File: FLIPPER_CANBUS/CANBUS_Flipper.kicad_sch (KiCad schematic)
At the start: 15 parts, among them J1 Conn_01x10_Socket, J2 Conn_01x08_Socket, J3 Conn_01x02, U1 MCP2515-xST, U2 MAX3051, Y1 16 Mhz

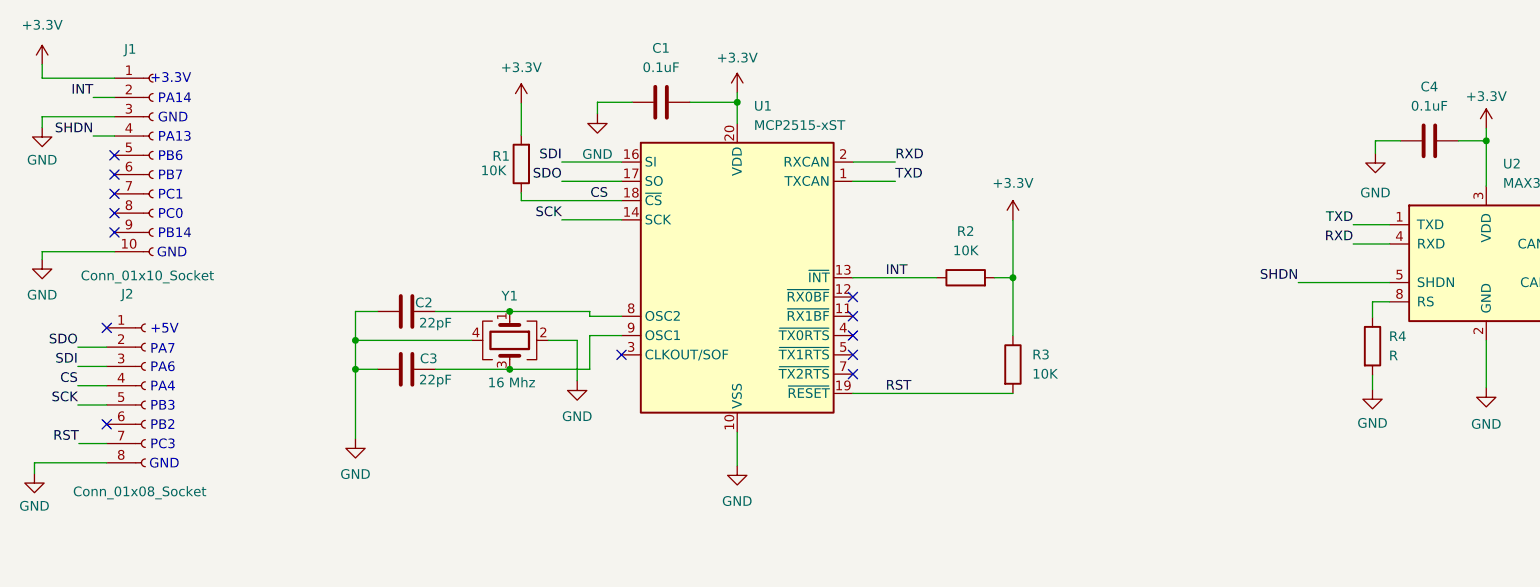
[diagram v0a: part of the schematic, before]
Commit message: Resistance Correction
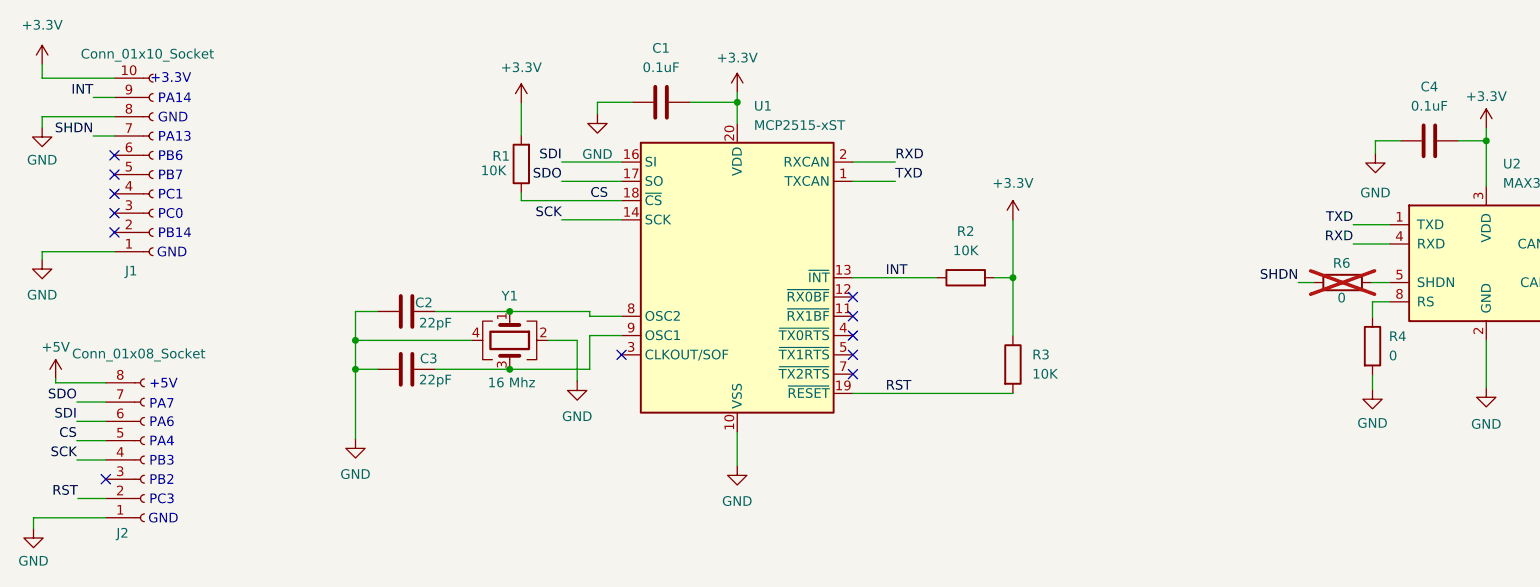
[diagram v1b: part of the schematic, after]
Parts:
- added R6: 0, symbol Device:R
- C1, C4: LCSC# (none) -> C14663; Manufactura (none) -> LCSC; manf# (none) -> CC0603KRX7R9BB104
- C2, C3: LCSC# (none) -> C91701; Manufactura (none) -> LCSC; manf# (none) -> 0603CG220J500NT
- J1: LCSC# (none) -> C5224020; Manufactura (none) -> LCSC; manf# (none) -> PZ2.54-1*10-FWZ
- J2: LCSC# (none) -> C18164984; Manufactura (none) -> LCSC; manf# (none) -> DS1025-02-1x8P8BR1-B
- J3: Manufactura (none) -> Steren; manf# (none) -> TRT-02
- R1, R2, R3: LCSC# (none) -> C217281; Manufactura (none) -> LCSC; manf# (none) -> CR-03JL7---10K
- R4: value R -> 0; LCSC# (none) -> C163836; Manufactura (none) -> LCSC; manf# (none) -> WR06X0000FTL
- R5: LCSC# (none) -> C2828631; Manufactura (none) -> LCSC; manf# (none) -> AR03BTCX1200
- U1: LCSC# (none) -> C15193; Manufactura (none) -> LCSC; manf# (none) -> MCP2515-I/ST
- U2: LCSC# (none) -> C112005; Manufactura (none) -> LCSC; manf# (none) -> MAX3051EKA+T
- Y1: LCSC# (none) -> C254270; Manufactura (none) -> LCSC; manf# (none) -> X2C016000B91H-R
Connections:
- net +3.3V: now also J1.10 (Pin_10); no longer J1.1 (Pin_1)
- net CS: now also J2.5 (Pin_5); no longer J2.4 (Pin_4)
- net GND: now also J1.1 (Pin_1), J1.8 (Pin_8), J2.1 (Pin_1); no longer J1.10 (Pin_10), J1.3 (Pin_3), J2.8 (Pin_8)
- net INT: now also J1.9 (Pin_9); no longer J1.2 (Pin_2)
- net RST: now also J2.2 (Pin_2); no longer J2.7 (Pin_7)
- net SCK: now also J2.4 (Pin_4); no longer J2.5 (Pin_5)
- net SDI: now also J2.6 (Pin_6); no longer J2.3 (Pin_3)
- net SDO: now also J2.7 (Pin_7); no longer J2.2 (Pin_2)
- net SHDN: now also J1.7 (Pin_7), R6.1; no longer J1.4 (Pin_4), U2.5 (SHDN)
- new net: R6.2, U2.5 (SHDN)
- new net +5V: J2.8 (Pin_8)
- no-connect marks 13 -> 12
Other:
- moved on the sheet: J2

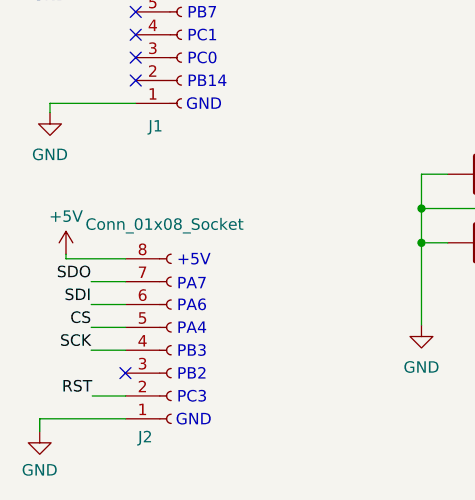
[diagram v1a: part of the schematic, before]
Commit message: feat(Hw):Update_pins_SDO_SDI
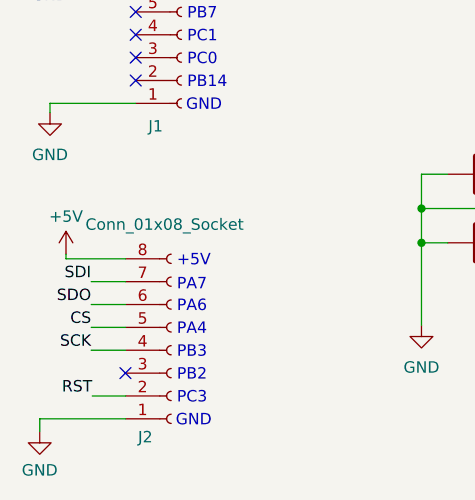
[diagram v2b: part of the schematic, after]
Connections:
- net SDI: now also J2.7 (Pin_7); no longer J2.6 (Pin_6)
- net SDO: now also J2.6 (Pin_6); no longer J2.7 (Pin_7)
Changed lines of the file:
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@@
     (effects (font (size 1.27 1.27)) (justify right bottom))
   )
-  (label "SDI" (at 43.053 73.279 180) (fields_autoplaced)
+  (label "SDI" (at 43.053 70.739 180) (fields_autoplaced)
     (effects (font (size 1.27 1.27)) (justify right bottom))
   )
@@
     (effects (font (size 1.27 1.27)) (justify right bottom))
   )
-  (label "SDO" (at 43.053 70.739 180) (fields_autoplaced)
+  (label "SDO" (at 43.053 73.279 180) (fields_autoplaced)
     (effects (font (size 1.27 1.27)) (justify right bottom))
   )

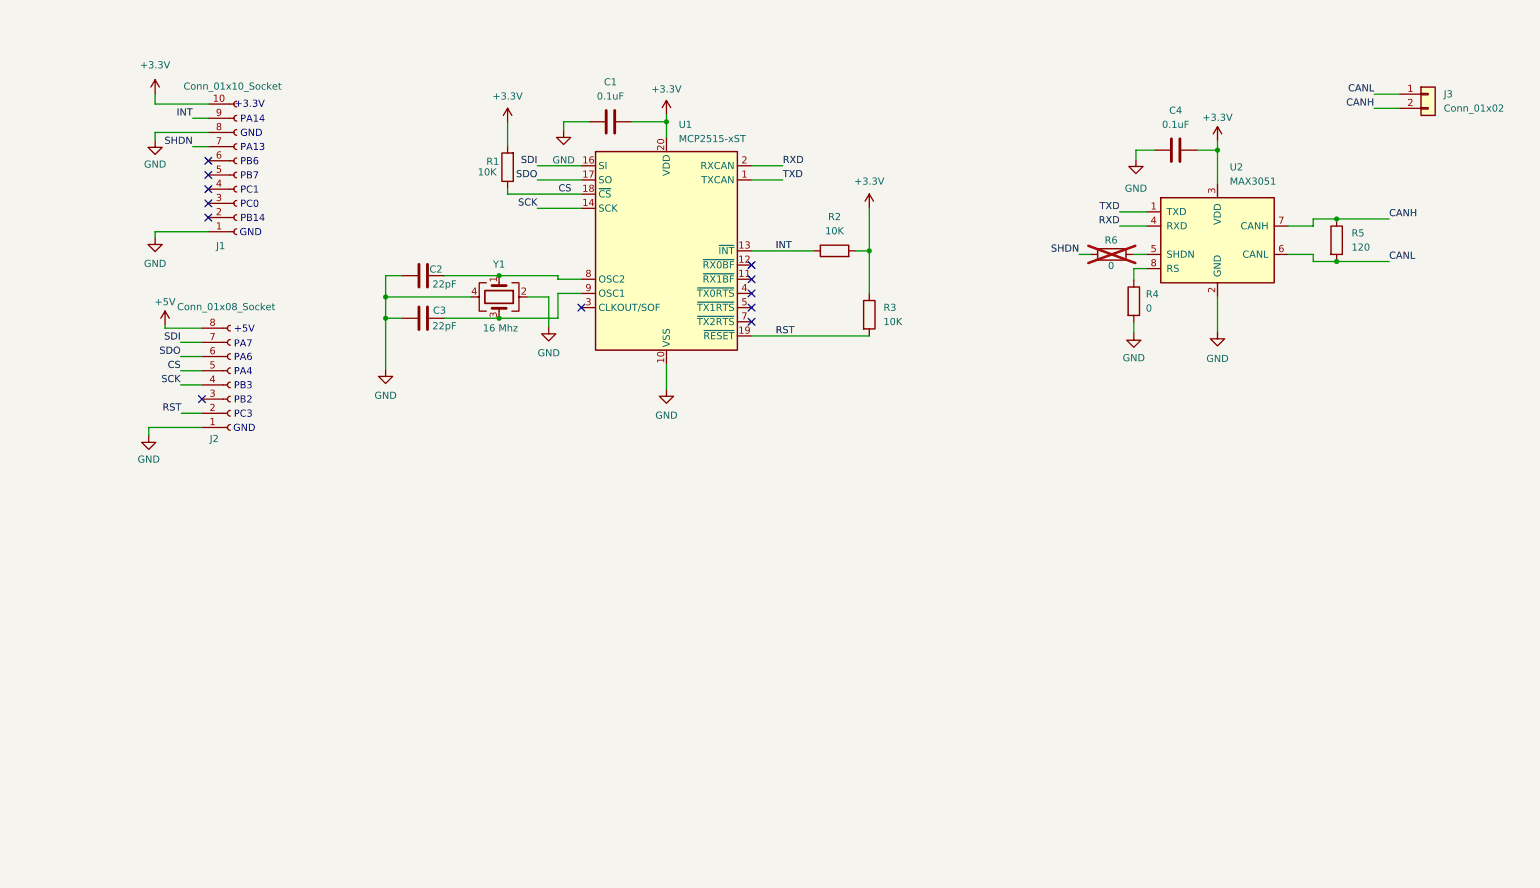
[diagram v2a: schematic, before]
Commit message: feat(hw):Canbus Shield jumper added
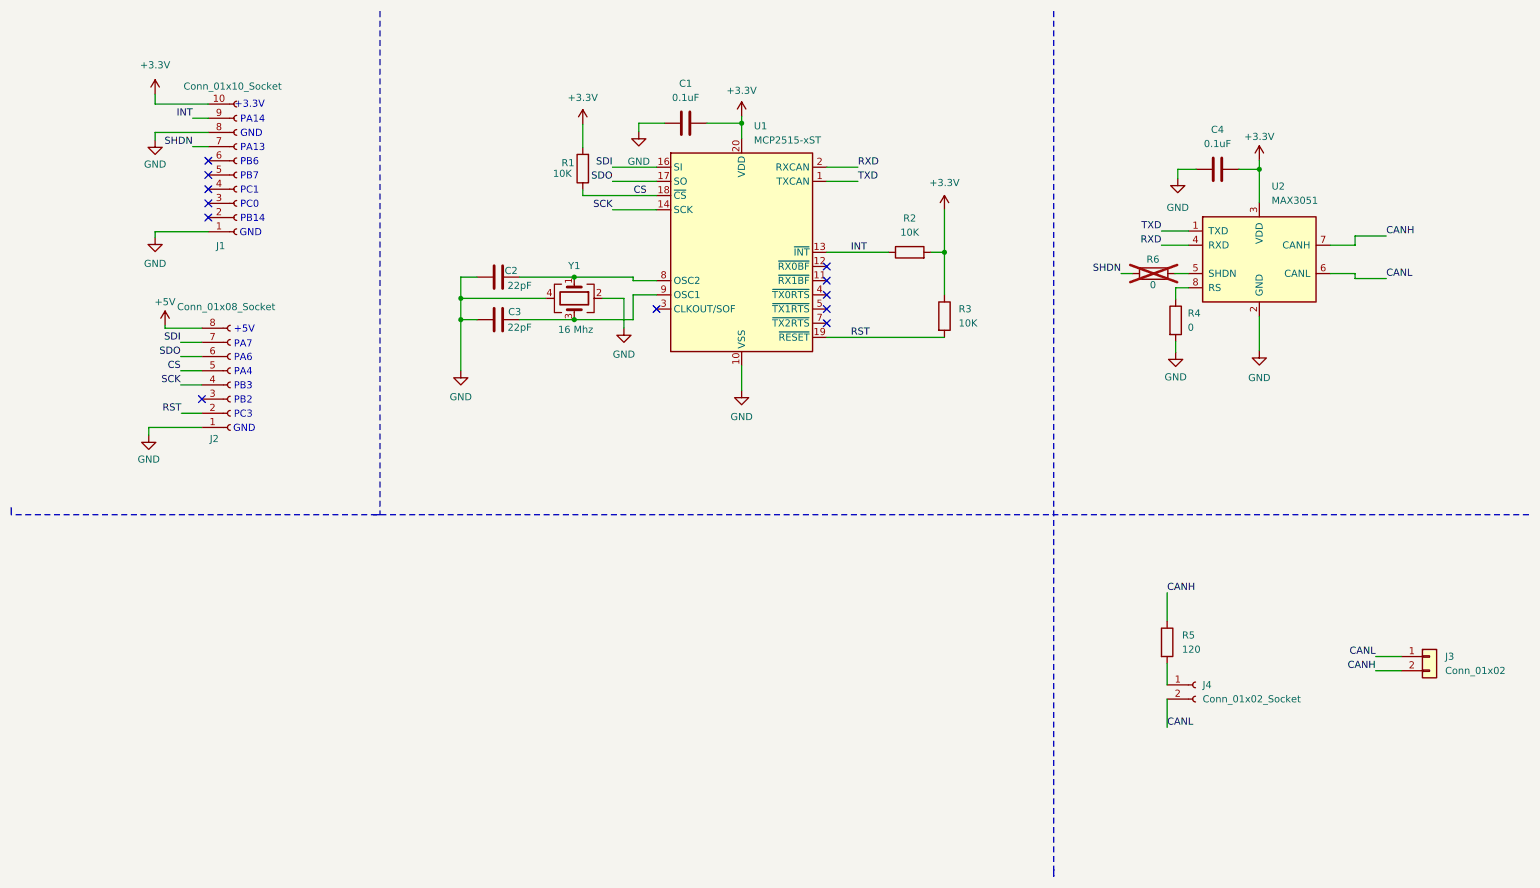
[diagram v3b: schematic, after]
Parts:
- added J4: Conn_01x02_Socket, Connector_PinHeader_2.54mm:PinHeader_1x02_P2.54mm_Vertical, symbol Connector:Conn_01x02_Socket
- C1, C2, C3, C4: footprint Capacitor_SMD:C_0603_1608Metric_Pad1.05x0.95mm_HandSolder -> Capacitor_SMD:C_0603_1608Metric_Pad1.08x0.95mm_HandSolder
- R1, R2, R3, R5: footprint Resistor_SMD:R_0603_1608Metric_Pad1.05x0.95mm_HandSolder -> Resistor_SMD:R_0603_1608Metric_Pad0.98x0.95mm_HandSolder
- R4, R6: footprint (none) -> Resistor_SMD:R_0603_1608Metric_Pad0.98x0.95mm_HandSolder
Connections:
- net CANL: now also J4.2 (Pin_2); no longer R5.2
- new net: J4.1 (Pin_1), R5.2
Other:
- moved on the sheet: C1, C2, C3, C4, J3, R1, R2, R3, R4, R5, R6, U1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

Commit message: feat(hw): Paths and jumper update
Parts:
- J4: footprint Connector_PinHeader_2.54mm:PinHeader_1x02_P2.54mm_Vertical -> Jumper:SolderJumper-2_P1.3mm_Open_TrianglePad1.0x1.5mm
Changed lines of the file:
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@@
       (effects (font (size 1.27 1.27)) (justify left))
     )
-    (property "Footprint" "Connector_PinHeader_2.54mm:PinHeader_1x02_P2.54mm_Vertical" (at 224.79 132.08 0)
+    (property "Footprint" "Jumper:SolderJumper-2_P1.3mm_Open_TrianglePad1.0x1.5mm" (at 224.79 132.08 0)
       (effects (font (size 1.27 1.27)) hide)
     )

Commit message: feat(hw): update design
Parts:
- J1: LCSC# C5224020 -> C7430366
- J2: LCSC# C18164984 -> C7501586
- J4: now not fitted
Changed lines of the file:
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@@
   )
   (symbol (lib_id "Connector:Conn_01x02_Socket") (at 224.79 132.08 0) (unit 1)
-    (in_bom yes) (on_board yes) (dnp no) (fields_autoplaced)
+    (in_bom yes) (on_board yes) (dnp yes) (fields_autoplaced)
     (property "Reference" "J4" (at 226.06 132.08 0)
       (effects (font (size 1.27 1.27)) (justify left))
@@
       (effects (font (size 1.27 1.27)) hide)
     )
-    (property "Datasheet" "https://datasheet.lcsc.com/lcsc/2210311700_ZHOURI-PZ2-54-1-10-FWZ_C5224020.pdf" (at 53.086 40.767 0)
-      (effects (font (size 1.27 1.27)) hide)
-    )
-    (property "LCSC#" "C5224020" (at 53.086 40.767 0)
+    (property "Datasheet" "https://www.lcsc.com/datasheet/lcsc_datasheet_2312310521_CONNFLY-Elec-DS1021-1x10SF11-B_C7430366.pdf" (at 53.086 40.767 0)
+      (effects (font (size 1.27 1.27)) hide)
+    )
+    (property "LCSC#" "C7430366" (at 53.086 40.767 0)
       (effects (font (size 1.27 1.27)) hide)
     )
@@
       (effects (font (size 1.27 1.27)) hide)
     )
-    (property "Datasheet" "https://datasheet.lcsc.com/lcsc/2309151604_CONNFLY-Elec-DS1025-02-1x8P8BR1-B_C18164984.pdf" (at 51.943 78.359 0)
-      (effects (font (size 1.27 1.27)) hide)
-    )
-    (property "LCSC#" "C18164984" (at 51.943 78.359 0)
-      (effects (font (size 1.27 1.27)) hide)
-    )
+    (property "Datasheet" "https://www.lcsc.com/datasheet/lcsc_datasheet_2401281115_XUNPU-PH2-54-01-08PZD_C7501586.pdf" (at 51.943 78.359 0)
+      (effects (font (size 1.27 1.27)) hide)
+    )
+    (property "LCSC#" "C7501586" (at 51.943 78.359 0)
+      (effects (font (size 1.27 1.27)) hide)
+    )

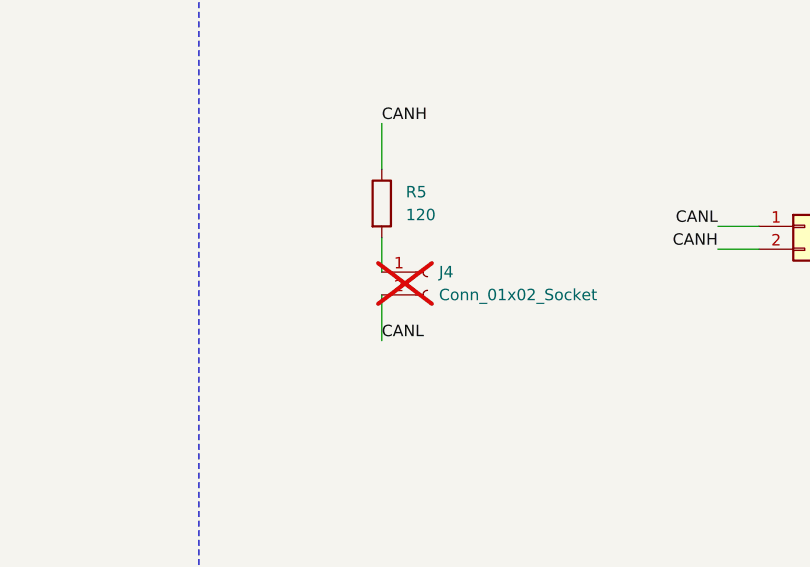
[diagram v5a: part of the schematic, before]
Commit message: feat(hw): jumper changed and bom added
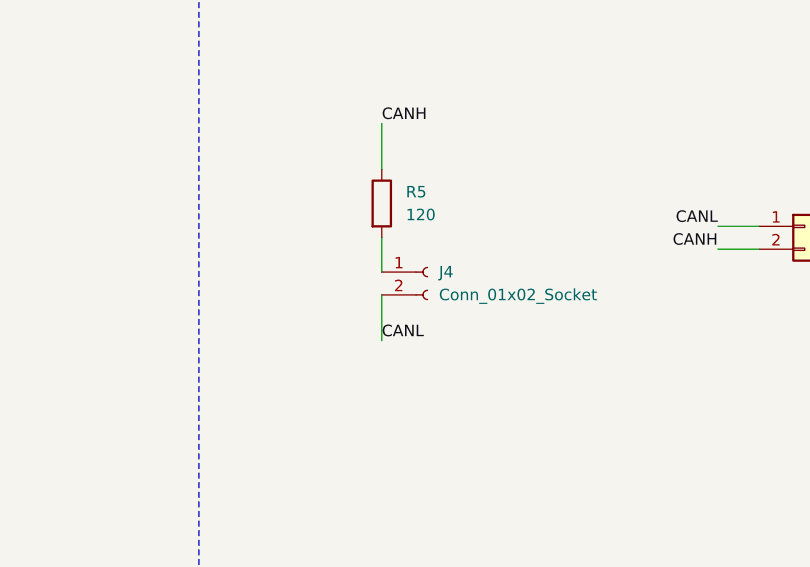
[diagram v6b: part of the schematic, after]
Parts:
- J1: manf# PZ2.54-1*10-FWZ -> DS1021-1x10SF11-B
- J2: manf# DS1025-02-1x8P8BR1-B -> PH2.54-01-08PZD
- J4: footprint Jumper:SolderJumper-2_P1.3mm_Open_TrianglePad1.0x1.5mm -> Connector_PinHeader_2.54mm:PinHeader_1x02_P2.54mm_Vertical; LCSC# (none) -> C7501580; Manufactura (none) -> LCSC; manf# (none) -> PH2.54-01-02PZD; now fitted
- R1, R2, R3: manf# CR-03JL7---10K -> WR06X0000FTL
- R4, R6: manf# WR06X0000FTL -> AR03BTCX1200
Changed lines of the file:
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@@
   )
   (symbol (lib_id "Connector:Conn_01x02_Socket") (at 224.79 132.08 0) (unit 1)
-    (in_bom yes) (on_board yes) (dnp yes) (fields_autoplaced)
+    (in_bom yes) (on_board yes) (dnp no) (fields_autoplaced)
     (property "Reference" "J4" (at 226.06 132.08 0)
       (effects (font (size 1.27 1.27)) (justify left))
@@
       (effects (font (size 1.27 1.27)) (justify left))
     )
-    (property "Footprint" "Jumper:SolderJumper-2_P1.3mm_Open_TrianglePad1.0x1.5mm" (at 224.79 132.08 0)
-      (effects (font (size 1.27 1.27)) hide)
-    )
-    (property "Datasheet" "~" (at 224.79 132.08 0)
+    (property "Footprint" "Connector_PinHeader_2.54mm:PinHeader_1x02_P2.54mm_Vertical" (at 224.79 132.08 0)
+      (effects (font (size 1.27 1.27)) hide)
+    )
+    (property "Datasheet" "https://www.lcsc.com/datasheet/lcsc_datasheet_2401281145_XUNPU-PH2-54-01-02PZD_C7501580.pdf" (at 224.79 132.08 0)
+      (effects (font (size 1.27 1.27)) hide)
+    )
+    (property "LCSC#" "C7501580" (at 224.79 132.08 0)
+      (effects (font (size 1.27 1.27)) hide)
+    )
+    (property "Manufactura" "LCSC" (at 224.79 132.08 0)
+      (effects (font (size 1.27 1.27)) hide)
+    )
+    (property "manf#" "PH2.54-01-02PZD" (at 224.79 132.08 0)
       (effects (font (size 1.27 1.27)) hide)
     )
@@
       (effects (font (size 1.27 1.27)) hide)
     )
-    (property "manf#" "CR-03JL7---10K" (at 115.062 39.624 0)
+    (property "manf#" "WR06X0000FTL" (at 115.062 39.624 0)
       (effects (font (size 1.27 1.27)) hide)
     )
@@
       (effects (font (size 1.27 1.27)) hide)
     )
-    (property "manf#" "WR06X0000FTL" (at 217.297 58.42 0)
+    (property "manf#" "AR03BTCX1200" (at 217.297 58.42 0)
       (effects (font (size 1.27 1.27)) hide)
     )
@@
       (effects (font (size 1.27 1.27)) hide)
     )
-    (property "manf#" "CR-03JL7---10K" (at 179.832 66.04 0)
+    (property "manf#" "WR06X0000FTL" (at 179.832 66.04 0)
       (effects (font (size 1.27 1.27)) hide)
     )
@@
       (effects (font (size 1.27 1.27)) hide)
     )
-    (property "manf#" "WR06X0000FTL" (at 221.234 66.802 0)
+    (property "manf#" "AR03BTCX1200" (at 221.234 66.802 0)
       (effects (font (size 1.27 1.27)) hide)
     )
@@
       (effects (font (size 1.27 1.27)) hide)
     )
-    (property "manf#" "PZ2.54-1*10-FWZ" (at 53.086 40.767 0)
+    (property "manf#" "DS1021-1x10SF11-B" (at 53.086 40.767 0)
       (effects (font (size 1.27 1.27)) hide)
     )
@@
       (effects (font (size 1.27 1.27)) hide)
     )
-    (property "manf#" "CR-03JL7---10K" (at 173.609 54.61 0)
+    (property "manf#" "WR06X0000FTL" (at 173.609 54.61 0)
       (effects (font (size 1.27 1.27)) hide)
     )
@@
       (effects (font (size 1.27 1.27)) hide)
     )
-    (property "manf#" "DS1025-02-1x8P8BR1-B" (at 51.943 78.359 0)
-      (effects (font (size 1.27 1.27)) hide)
-    )
+    (property "manf#" "PH2.54-01-08PZD" (at 51.943 78.359 0)
+      (effects (font (size 1.27 1.27)) hide)
+    )

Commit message: fix(hw): CANBUS shiled bom modified
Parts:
- R1, R2, R3: manf# WR06X0000FTL -> CR-03JL7---10K
- R4, R6: manf# AR03BTCX1200 -> WR06X0000FTL
